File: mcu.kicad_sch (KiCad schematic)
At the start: 1 part, among them U1 STM32F446VETx

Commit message: Power rail stuff
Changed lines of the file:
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@@
 		(in_pos_files yes)
 		(dnp no)
-		(fields_autoplaced yes)
 		(property "Reference" "U1"
-			(at 135.6548 172.72 0)
+			(at 149.098 35.814 0)
 			(show_name no)
 			(do_not_autoplace no)
@@
 		)
 		(property "Value" "STM32F446VETx"
-			(at 135.6548 175.26 0)
+			(at 137.668 172.466 0)
 			(show_name no)
 			(do_not_autoplace no)
@@
 		(instances
 			(project "modretrocon"
-				(path "/4f4dfd23-e96d-40a8-91c2-e53fb8a1f2eb"
-					(reference "U1")
-					(unit 1)
-				)
-			)
-			(project "modretrocon"
 				(path "/cf6749e4-132f-4e26-b0d6-92782ee54bed/4d59c3d8-a5c2-4135-9570-fdfaf506da3f"

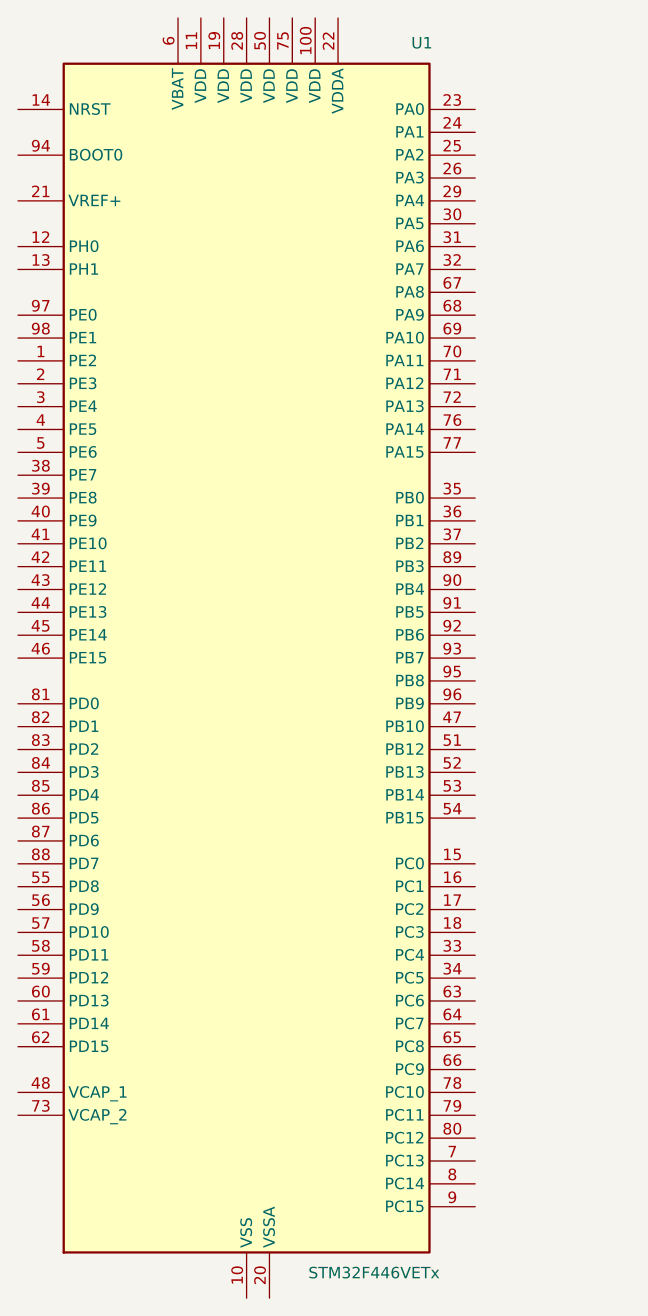
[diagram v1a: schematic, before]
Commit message: Fixed regulator, started wiring the microSD & MCU
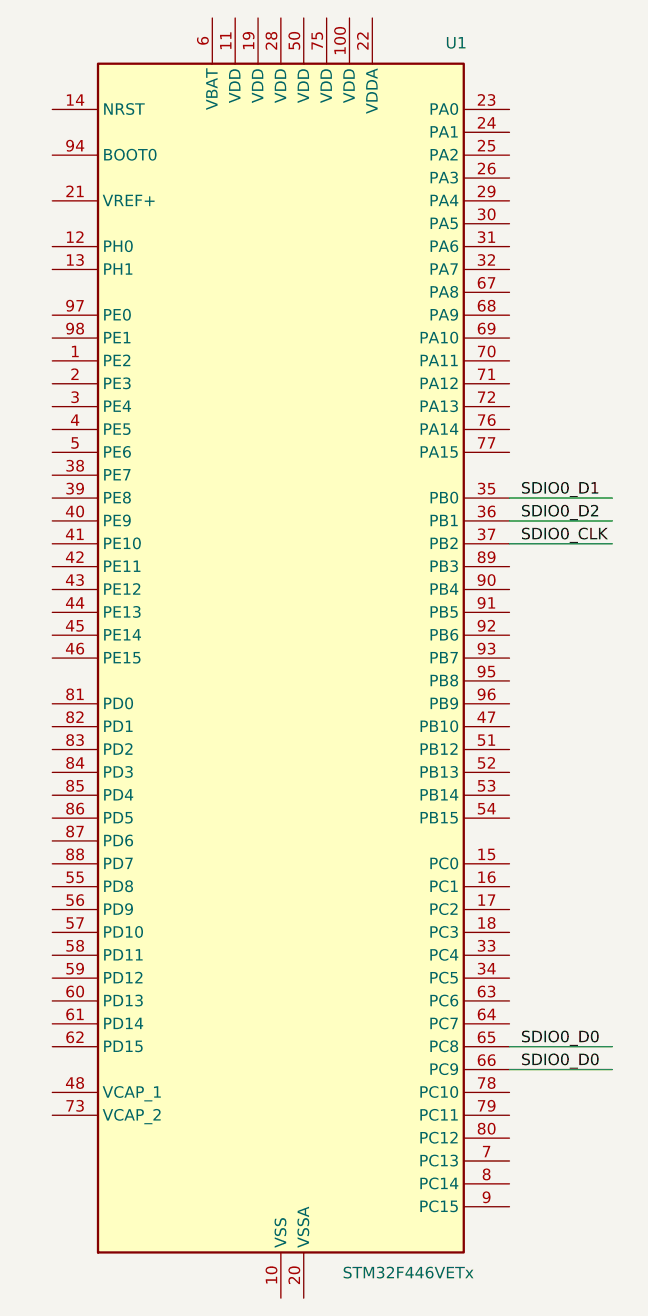
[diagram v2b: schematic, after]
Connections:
- net SDIO0_D1: now reaches U1.35 (PB0)
- net SDIO0_D2: now reaches U1.36 (PB1)
- net SDIO0_CLK: now reaches U1.37 (PB2)
- net SDIO0_D0: now reaches U1.65 (PC8)
- net SDIO0_D0: now also U1.66 (PC9)
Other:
- moved on the sheet: U1
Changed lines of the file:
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@@
 		(company "Carbine")
+	)
+	(wire
+		(pts
+			(xy 160.02 88.9) (xy 171.45 88.9)
+		)
+		(stroke
+			(width 0)
+			(type default)
+		)
+	)
+	(wire
+		(pts
+			(xy 160.02 149.86) (xy 171.45 149.86)
+		)
+		(stroke
+			(width 0)
+			(type default)
+		)
+	)
+	(wire
+		(pts
+			(xy 160.02 91.44) (xy 171.45 91.44)
+		)
+		(stroke
+			(width 0)
+			(type default)
+		)
+	)
+	(wire
+		(pts
+			(xy 160.02 147.32) (xy 171.45 147.32)
+		)
+		(stroke
+			(width 0)
+			(type default)
+		)
+	)
+	(wire
+		(pts
+			(xy 160.02 86.36) (xy 171.45 86.36)
+		)
+		(stroke
+			(width 0)
+			(type default)
+		)
+	)
+	(label "SDIO0_D2"
+		(at 161.29 88.9 0)
+		(effects
+			(font
+				(size 1.27 1.27)
+			)
+			(justify left bottom)
+		)
+	)
+	(label "SDIO0_D0"
+		(at 161.29 149.86 0)
+		(effects
+			(font
+				(size 1.27 1.27)
+			)
+			(justify left bottom)
+		)
+	)
+	(label "SDIO0_CLK"
+		(at 161.29 91.44 0)
+		(effects
+			(font
+				(size 1.27 1.27)
+			)
+			(justify left bottom)
+		)
+	)
+	(label "SDIO0_D1"
+		(at 161.29 86.36 0)
+		(effects
+			(font
+				(size 1.27 1.27)
+			)
+			(justify left bottom)
+		)
+	)
+	(label "SDIO0_D0"
+		(at 161.29 147.32 0)
+		(effects
+			(font
+				(size 1.27 1.27)
+			)
+			(justify left bottom)
+		)
 	)
 	(symbol
 		(lib_id "MCU_ST_STM32F4:STM32F446VETx")
-		(at 130.81 104.14 0)
+		(at 134.62 104.14 0)
 		(unit 1)
 		(body_style 1)
@@
 		(dnp no)
 		(property "Reference" "U1"
-			(at 149.098 35.814 0)
+			(at 152.908 35.814 0)
 			(show_name no)
 			(do_not_autoplace no)
@@
 		)
 		(property "Value" "STM32F446VETx"
-			(at 137.668 172.466 0)
+			(at 141.478 172.466 0)
 			(show_name no)
 			(do_not_autoplace no)
@@
 		)
 		(property "Footprint" "Package_QFP:LQFP-100_14x14mm_P0.5mm"
-			(at 110.49 170.18 0)
+			(at 114.3 170.18 0)
 			(hide yes)
 			(show_name no)
@@
 		)
 		(property "Datasheet" "https://www.st.com/resource/en/datasheet/stm32f446ve.pdf"
-			(at 130.81 104.14 0)
+			(at 134.62 104.14 0)
 			(hide yes)
 			(show_name no)
@@
 		)
 		(property "Description" "STMicroelectronics Arm Cortex-M4 MCU, 512KB flash, 128KB RAM, 180 MHz, 1.8-3.6V, 81 GPIO, LQFP100"
-			(at 130.81 104.14 0)
+			(at 134.62 104.14 0)
 			(hide yes)
 			(show_name no)

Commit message: MCU wiring
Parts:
- removed U1: STM32F446VETx, Package_QFP:LQFP-100_14x14mm_P0.5mm, symbol MCU_ST_STM32F4:STM32F446VETx
- added C17, C18, C19, C20, C21, C22, C23, C24, C25, C26, C27, C28, C30, C31, C32, C34: 100n, symbol Device:C_Small
- added C29, C33, C35: 4.7u, symbol Device:C_Small
- added C36: 2.2u, symbol Device:C_Small
- added L5: L_Ferrite, symbol Device:L_Ferrite
- added R10: 47, symbol Device:R_US
- added U2: STM32F429ZITx, Package_QFP:LQFP-144_20x20mm_P0.5mm, symbol MCU_ST_STM32F4:STM32F429ZITx
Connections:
- new net: C17.1, C18.1, C19.1, C20.1, C21.1, C22.1, C23.2, C24.2, C25.2, C26.2, C27.2, C28.2, C29.1, C30.2
- new net: R10.2, U2.32 (VREF+)
- new net: C35.1, U2.106 (VCAP_2), U2.71 (VCAP_1)
- new net: C35.2, C36.2
- new net +3.3V: C17.2, C18.2, C19.2, C20.2, C21.2, C22.2, C23.1, C24.1, C25.1, C26.1, C27.1, C28.1, C29.2, C30.1, C31.1, C31.2, C32.2, C33.2, C34.2, C36.1, L5.1, U2.107 (VSS), U2.108 (VDD), U2.120 (VSS), U2.121 (VDD), U2.130 (VSS), U2.131 (VDD), U2.144 (VDD), U2.16 (VSS), U2.17 (VDD), U2.30 (VDD), U2.31 (VSSA), U2.38 (VSS), U2.39 (VDD), U2.51 (VSS), U2.52 (VDD), U2.6 (VBAT), U2.61 (VSS), U2.62 (VDD), U2.72 (VDD), U2.83 (VSS), U2.84 (VDD), U2.94 (VSS), U2.95 (VDD)
- new net MCU_VDDA: C32.1, C33.1, C34.1, L5.2, R10.1, U2.33 (VDDA)

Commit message: Minor
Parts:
- C29: value 4.7u -> 10u
- C33: value 4.7u -> 1u
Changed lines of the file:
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@@
 			)
 		)
-		(property "Value" "4.7u"
+		(property "Value" "1u"
 			(at 60.96 73.6663 0)
 			(show_name no)
@@
 			)
 		)
-		(property "Value" "4.7u"
+		(property "Value" "10u"
 			(at 27.94 44.4563 0)
 			(show_name no)

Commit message: Minor
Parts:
- added C39: 0.1u, symbol Device:C_Small
- added C40, C44: 10u, symbol Device:C_Small
- added C41: 4.7u, symbol Device:C_Small
- added C42, C43: 100n, symbol Device:C_Small
- added R11: 47, symbol Device:R_US
- added SW2: SW_SPDT, symbol Switch:SW_SPDT
- added Y3: Crystal_GND24, symbol Device:Crystal_GND24
- R10: value 47 -> 10k
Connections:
- net +3.3V: now also R10.2, U2.143 (PDR_ON), C39.1, C40.1, C41.2, C42.2, C44.2, SW2.3 (C), Y3.2 (G), Y3.4 (G)
- net VREF_P: now reaches U2.32 (VREF+)
- net VREF_P: now also C43.1, C43.2, R11.2; no longer R10.2
- net BOOT0: now reaches U2.138 (BOOT0)
- net BOOT0: now also R10.1, SW2.2 (B)
- net XTAL_P: now reaches U2.23 (PH0)
- net XTAL_P: now also C40.2, Y3.1
- net XTAL_N: now reaches U2.24 (PH1)
- net XTAL_N: now also C44.1, Y3.3
- net MCU_NRST: now reaches U2.25 (NRST)
- net MCU_NRST: now also C39.2
- net MCU_VDDA renamed +3.3VA
- net +3.3VA: now also C41.1, C42.1, R11.1; no longer R10.1
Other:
- note added: "Move to Power?"
- note added: "TODO: Choose a part & its load cap"
